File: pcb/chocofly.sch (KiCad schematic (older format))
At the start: 142 parts, among them P1 battery+, P2 battery-, SW1 SW_Push, SW11 SW_Push, SW12 SW_Push, SW13 SW_Push, SW14 SW_Push, SW15 SW_Push, SW16 SW_Push, SW17 SW_Push, SW18 SW_Push, SW19 SW_Push, SW2 SW_Push, SW20 SW_Push, SW21 SW_Push, SW22 SW_Push, SW23 SW_Push, SW24 SW_Push, SW25 SW_Push, SW26 SW_Push, SW27 SW_Push, SW28 SW_Push, SW29 SW_Push, SW3 SW_Push, SW30 SW_Push, SW31 SW_Push, SW32 SW_Push, SW33 SW_Push, SW34 SW_Push, SW35 SW_Push, SW36 SW_Push, SW37 SW_Push, SW38 SW_Push, SW39 SW_Push, SW4 SW_Push, SW40 SW_Push, SW41 SW_Push, SW42 SW_Push, SW43 SW_Push, SW44 SW_Push, SW45 SW_Push, SW46 SW_Push, SW47 SW_Push, SW48 SW_Push, SW49 SW_Push, SW5 SW_Push, SW50 SW_Push, SW51 SW_Push, SW52 SW_Push, SW53 SW_Push, SW54 SW_Push, SW55 SW_Push, SW56 SW_Push, SW57 SW_Push, SW58 SW_Push, SW59 SW_Push, SW6 SW_Push, SW60 SW_Push, SW61 SW_Push, SW62 Reset, SW63 Power, SW7 SW_Push, SW8 SW_Push, SW9 SW_Push

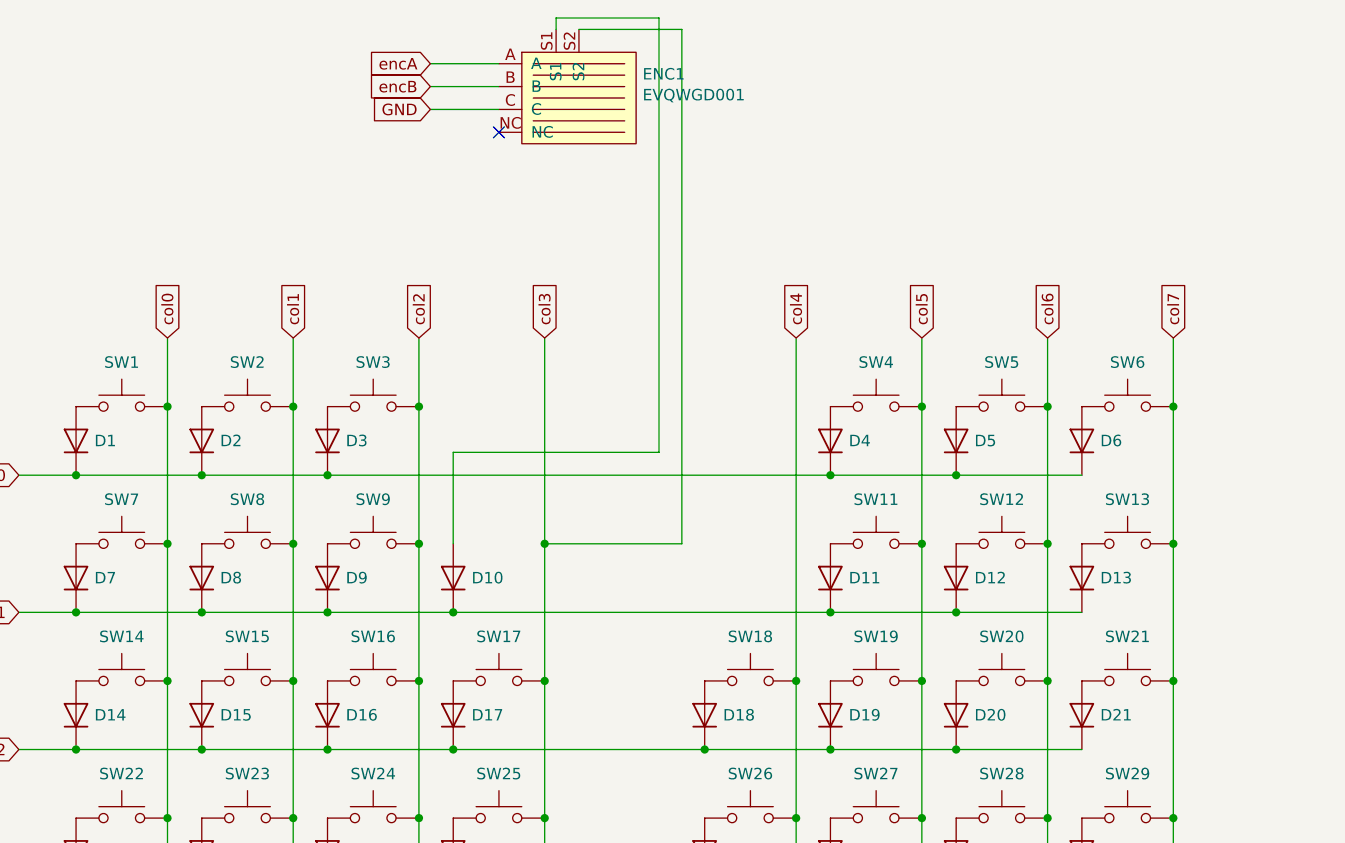
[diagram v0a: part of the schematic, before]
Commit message: Added one more encoder
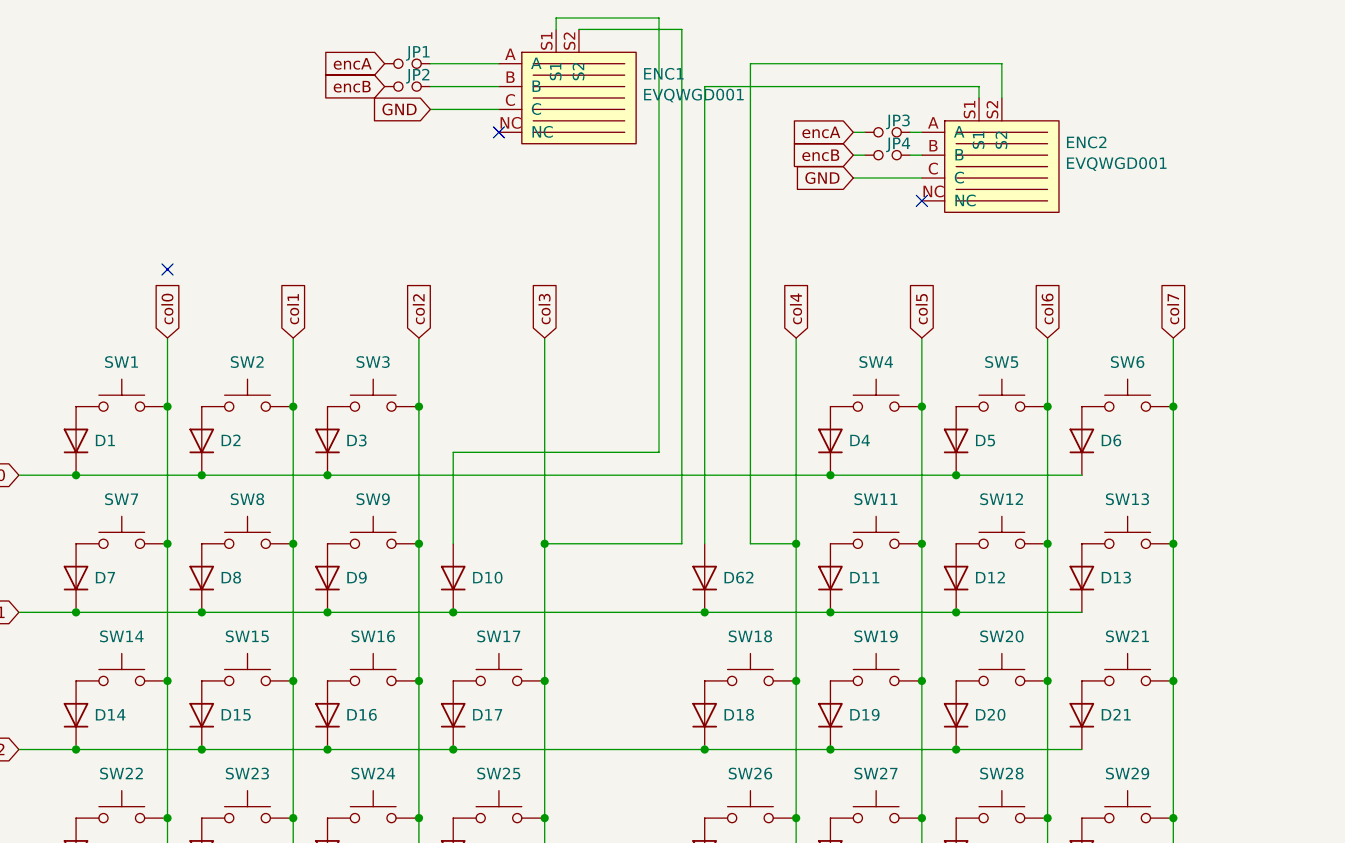
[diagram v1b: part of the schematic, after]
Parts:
- added D62: 1N4148, footprints:diode_TH_SMD, symbol Diode:1N4148
- added ENC2: EVQWGD001, footprints:EVQWGD001, symbol evqwgd001:EVQWGD001
- added JP1, JP2, JP3, JP4: Jumper_NC_Small, footprints:avalanche_Jumper, symbol Device:Jumper_NO_Small
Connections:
- net GND: now also ENC2.C
- net col4: now also ENC2.S2
- net encA: now also JP1.1, JP3.1; no longer ENC1.A
- net encB: now also JP2.1, JP4.1; no longer ENC1.B
- net row1: now also D62.1 (K)
- new net: ENC1.A, JP1.2
- new net: ENC1.B, JP2.2
- new net: ENC2.A, JP3.2
- new net: ENC2.B, JP4.2
- new net: D62.2 (A), ENC2.S1
- no-connect marks 3 -> 5
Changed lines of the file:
@@
 Wire Wire Line
 	3400 1950 3400 2850
-Text GLabel 2900 850  0    50   Input ~ 0
+Text GLabel 2700 850  0    50   Input ~ 0
 encB
-Text GLabel 2900 750  0    50   Input ~ 0
+Text GLabel 2700 750  0    50   Input ~ 0
 encA
 Wire Wire Line
 	3000 2450 3000 2850
 Wire Wire Line
-	4500 1950 4500 3450
+	4500 1950 4500 2850
 Wire Wire Line
 	2450 2550 4650 2550
@@
 Connection ~ 4650 3150
 Wire Wire Line
-	3000 3150 4650 3150
+	3000 3150 4100 3150
 Wire Wire Line
 	3000 6750 4100 6750
@@
 NoConn ~ 3200 1050
 Wire Wire Line
+	2900 850  3200 850
+Wire Wire Line
+	2900 950  3200 950
+Wire Wire Line
+	2900 750  3200 750
+Text GLabel 4750 1150 0    50   Input ~ 0
+encB
+Text GLabel 4750 1050 0    50   Input ~ 0
+encA
+$Comp
+L evqwgd001:EVQWGD001 ENC2
+U 1 1 63C5D79B
+P 5400 1150
+F 0 "ENC2" H 5678 1204 50  0000 L CNN
+F 1 "EVQWGD001" H 5678 1113 50  0000 L CNN
+F 2 "footprints:EVQWGD001" H 5400 1150 50  0001 C CNN
+F 3 "" H 5400 1150 50  0001 C CNN
+	1    5400 1150
+	1    0    0    -1
+$EndComp
+Text GLabel 4750 1250 0    50   Input ~ 0
+GND
+Wire Wire Line
+	5300 900  5300 850
+NoConn ~ 1750 1650
+Wire Wire Line
+	4750 1250 5050 1250
+$Comp
+L Device:Jumper_NO_Small JP2
+U 1 1 63D764A1
+P 2800 850
+F 0 "JP2" H 2850 900 50  0000 C CNN
+F 1 "Jumper_NC_Small" H 2800 971 50  0001 C CNN
+F 2 "footprints:avalanche_Jumper" H 2800 850 50  0001 C CNN
+F 3 "~" H 2800 850 50  0001 C CNN
+	1    2800 850
+	1    0    0    -1
+$EndComp
+$Comp
+L Device:Jumper_NO_Small JP1
+U 1 1 63DA7A93
+P 2800 750
+F 0 "JP1" H 2850 800 50  0000 C CNN
+F 1 "Jumper_NC_Small" H 2800 871 50  0001 C CNN
+F 2 "footprints:avalanche_Jumper" H 2800 750 50  0001 C CNN
+F 3 "~" H 2800 750 50  0001 C CNN
+	1    2800 750
+	1    0    0    -1
+$EndComp
+$Comp
+L Diode:1N4148 D62
+U 1 1 63DE32C4
+P 4100 3000
+F 0 "D62" V 4100 2920 50  0000 R CNN
+F 1 "1N4148" H 4100 3126 50  0001 C CNN
+F 2 "footprints:diode_TH_SMD" H 4100 2825 50  0001 C CNN
+F 3 "https://assets.nexperia.com/documents/data-sheet/1N4148_1N4448.pdf" H 4100 3000 50  0001 C CNN
+	1    4100 3000
+	0    -1   -1   0
+$EndComp
+Connection ~ 4100 3150
+Wire Wire Line
+	4100 3150 4650 3150
+Wire Wire Line
 	3900 550  3900 2450
 Wire Wire Line
 	4000 600  4000 2850
 Wire Wire Line
-	2900 850  3200 850
-Wire Wire Line
-	2900 950  3200 950
-Wire Wire Line
-	2900 750  3200 750
+	4300 2850 4500 2850
+Connection ~ 4500 2850
+Wire Wire Line
+	4500 2850 4500 3450
+Wire Wire Line
+	5300 850  4100 850
+Wire Wire Line
+	4100 850  4100 2850
+Wire Wire Line
+	5400 900  5400 750
+Wire Wire Line
+	5400 750  4300 750
+Wire Wire Line
+	4300 750  4300 2850
+$Comp
+L Device:Jumper_NO_Small JP4
+U 1 1 63EC2670
+P 4900 1150
+F 0 "JP4" H 4950 1200 50  0000 C CNN
+F 1 "Jumper_NC_Small" H 4900 1271 50  0001 C CNN
+F 2 "footprints:avalanche_Jumper" H 4900 1150 50  0001 C CNN
+F 3 "~" H 4900 1150 50  0001 C CNN
+	1    4900 1150
+	1    0    0    -1
+$EndComp
+$Comp
+L Device:Jumper_NO_Small JP3
+U 1 1 63EC2676
+P 4900 1050
+F 0 "JP3" H 4950 1100 50  0000 C CNN
+F 1 "Jumper_NC_Small" H 4900 1171 50  0001 C CNN
+F 2 "footprints:avalanche_Jumper" H 4900 1050 50  0001 C CNN
+F 3 "~" H 4900 1050 50  0001 C CNN
+	1    4900 1050
+	1    0    0    -1
+$EndComp
+Wire Wire Line
+	5050 1050 5000 1050
+Wire Wire Line
+	4800 1050 4750 1050
+Wire Wire Line
+	4800 1150 4750 1150
+Wire Wire Line
+	5050 1150 5000 1150
+NoConn ~ 5050 1350
 $EndSCHEMATC

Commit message: Ready to wire
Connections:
- net encA: now also JP1.2, JP3.2; no longer JP1.1, JP3.1
- net encB: now also JP2.2, JP4.2; no longer JP2.1, JP4.1
- net at ENC1.A: now also JP1.1; no longer JP1.2
- net at ENC1.B: now also JP2.1; no longer JP2.2
- net at ENC2.A: now also JP3.1; no longer JP3.2
- net at ENC2.B: now also JP4.1; no longer JP4.2
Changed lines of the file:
@@
 	5300 900  5300 850
 NoConn ~ 1750 1650
-Wire Wire Line
-	4750 1250 5050 1250
 $Comp
 L Device:Jumper_NO_Small JP2
@@
 F 3 "~" H 2800 850 50  0001 C CNN
 	1    2800 850
-	1    0    0    -1
+	-1   0    0    1
 $EndComp
 $Comp
@@
 F 3 "~" H 2800 750 50  0001 C CNN
 	1    2800 750
-	1    0    0    -1
+	-1   0    0    1
 $EndComp
 $Comp
@@
 F 3 "~" H 4900 1150 50  0001 C CNN
 	1    4900 1150
-	1    0    0    -1
+	-1   0    0    1
 $EndComp
 $Comp
@@
 F 3 "~" H 4900 1050 50  0001 C CNN
 	1    4900 1050
-	1    0    0    -1
+	-1   0    0    1
 $EndComp
 Wire Wire Line
@@
 	5050 1150 5000 1150
 NoConn ~ 5050 1350
+Wire Wire Line
+	4750 1250 5050 1250
 $EndSCHEMATC

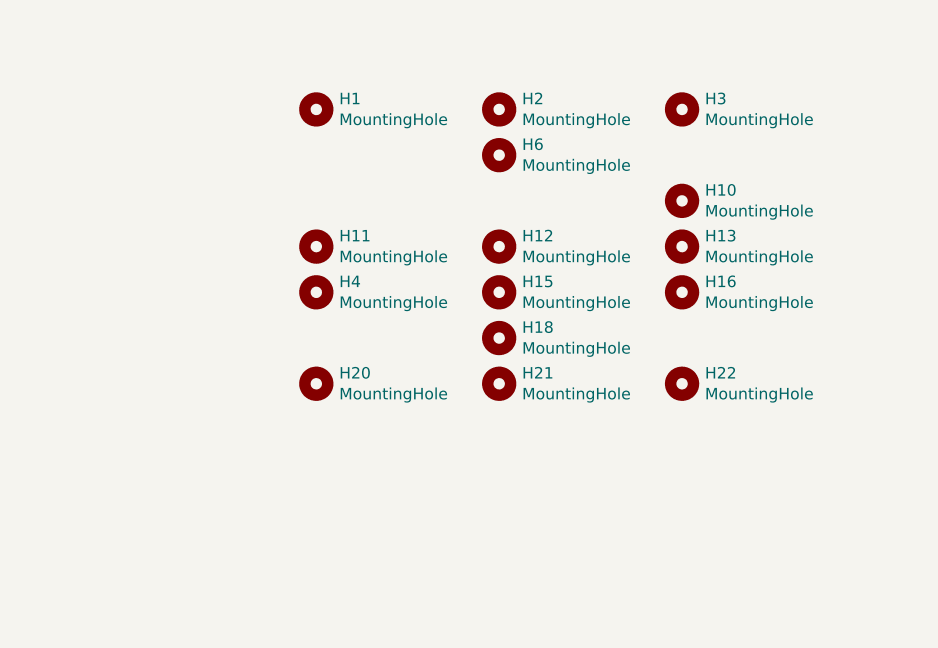
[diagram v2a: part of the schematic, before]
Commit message: New break-off way
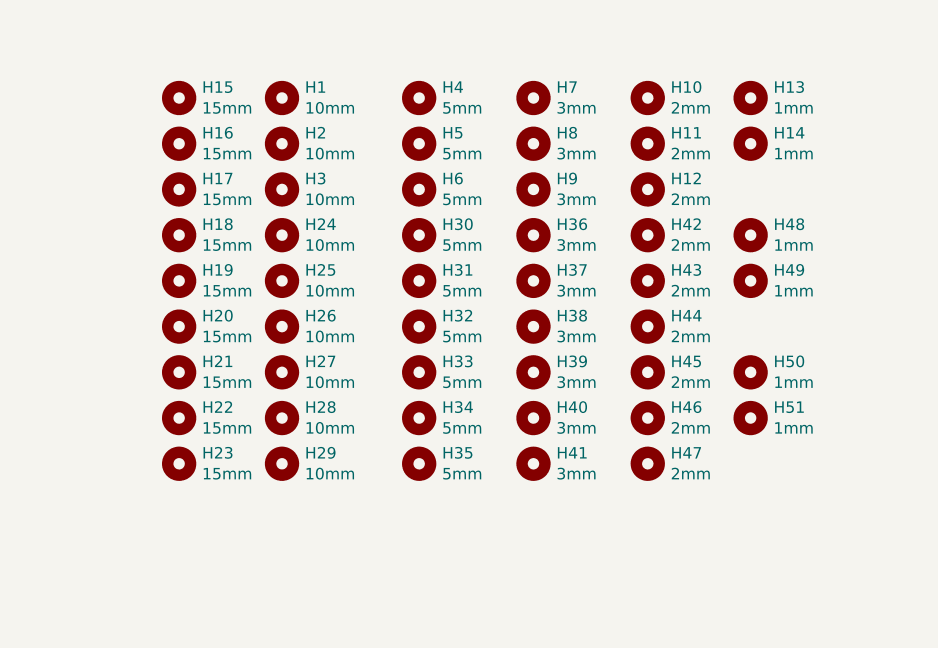
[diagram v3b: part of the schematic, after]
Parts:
- added H14, H48, H49, H50, H51: 1mm, footprints:hole_1mm, symbol Mechanical:MountingHole
- added H17, H19, H23: 15mm, footprints:hole_15mm, symbol Mechanical:MountingHole
- added H24, H25, H26, H27, H28, H29: 10mm, footprints:hole_10mm, symbol Mechanical:MountingHole
- added H30, H31, H32, H33, H34, H35, H5: 5mm, footprints:hole_5mm, symbol Mechanical:MountingHole
- added H36, H37, H38, H39, H40, H41, H7, H8, H9: 3mm, footprints:hole_3mm, symbol Mechanical:MountingHole
- added H42, H43, H44, H45, H46, H47: 2mm, footprints:hole_2mm, symbol Mechanical:MountingHole
- H1, H2, H3: value MountingHole -> 10mm; footprint MountingHole:MountingHole_2.2mm_M2 -> footprints:hole_10mm
- H10, H11, H12: value MountingHole -> 2mm; footprint MountingHole:MountingHole_2.2mm_M2 -> footprints:hole_2mm
- H13: value MountingHole -> 1mm; footprint MountingHole:MountingHole_2.2mm_M2 -> footprints:hole_1mm
- H15, H16, H18, H20, H21, H22: value MountingHole -> 15mm; footprint MountingHole:MountingHole_2.2mm_M2 -> footprints:hole_15mm
- H4, H6: value MountingHole -> 5mm; footprint MountingHole:MountingHole_2.2mm_M2 -> footprints:hole_5mm

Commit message: New egde cuts
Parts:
- removed H15, H16, H18, H20, H21, H23: 15mm, footprints:hole_15mm, symbol Mechanical:MountingHole
- removed H44, H47: 2mm, footprints:hole_2mm, symbol Mechanical:MountingHole
- added H52, H53, H54, H55, H56, H57, H58, H59, H61, H62: 3mm, footprints:hole_3mm, symbol Mechanical:MountingHole
- added H67: 1mm, footprints:hole_1mm, symbol Mechanical:MountingHole
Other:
- moved on the sheet: H10, H11, H12, H13, H14, H17, H19, H22, H42, H43, H45, H46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

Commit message: V2 is done
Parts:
- removed H22: 15mm, footprints:hole_15mm, symbol Mechanical:MountingHole
- removed H24: 10mm, footprints:hole_10mm, symbol Mechanical:MountingHole
- added H15, H16, H18: 2mm, footprints:hole_2mm, symbol Mechanical:MountingHole
- added H20: 5mm, footprints:hole_5mm, symbol Mechanical:MountingHole
- added H23, H44: 10mm, footprints:hole_10mm, symbol Mechanical:MountingHole
- added H47: 3mm, footprints:hole_3mm, symbol Mechanical:MountingHole
- H1: value 10mm -> 5mm; footprint footprints:hole_10mm -> footprints:hole_5mm
- H17: value 15mm -> 5mm; footprint footprints:hole_15mm -> footprints:hole_5mm
- H19: value 15mm -> 3mm; footprint footprints:hole_15mm -> footprints:hole_3mm
- H45: value 2mm -> 3mm; footprint footprints:hole_2mm -> footprints:hole_3mm
- H9: value 3mm -> 2mm; footprint footprints:hole_3mm -> footprints:hole_2mm
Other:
- moved on the sheet: H10, H11, H12, H13, H14, H2, H25, H26, H27, H28, H29, H3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

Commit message: Lots of minor changes
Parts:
- JP1, JP2: footprint footprints:avalanche_Jumper -> footprints:avalanche_Jumper_NC; symbol Device:Jumper_NO_Small -> Device:Jumper_NC_Small
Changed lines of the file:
@@
 NoConn ~ 1750 1650
 $Comp
-L Device:Jumper_NO_Small JP2
+L Device:Jumper_NC_Small JP2
 U 1 1 63D764A1
 P 2800 850
 F 0 "JP2" H 2850 900 50  0000 C CNN
 F 1 "Jumper_NC_Small" H 2800 971 50  0001 C CNN
-F 2 "footprints:avalanche_Jumper" H 2800 850 50  0001 C CNN
+F 2 "footprints:avalanche_Jumper_NC" H 2800 850 50  0001 C CNN
 F 3 "~" H 2800 850 50  0001 C CNN
 	1    2800 850
@@
 $EndComp
 $Comp
-L Device:Jumper_NO_Small JP1
+L Device:Jumper_NC_Small JP1
 U 1 1 63DA7A93
 P 2800 750
 F 0 "JP1" H 2850 800 50  0000 C CNN
 F 1 "Jumper_NC_Small" H 2800 871 50  0001 C CNN
-F 2 "footprints:avalanche_Jumper" H 2800 750 50  0001 C CNN
+F 2 "footprints:avalanche_Jumper_NC" H 2800 750 50  0001 C CNN
 F 3 "~" H 2800 750 50  0001 C CNN
 	1    2800 750
